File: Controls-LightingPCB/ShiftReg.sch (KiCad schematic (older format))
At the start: 1 part, among them U21 MCP23S17_SO

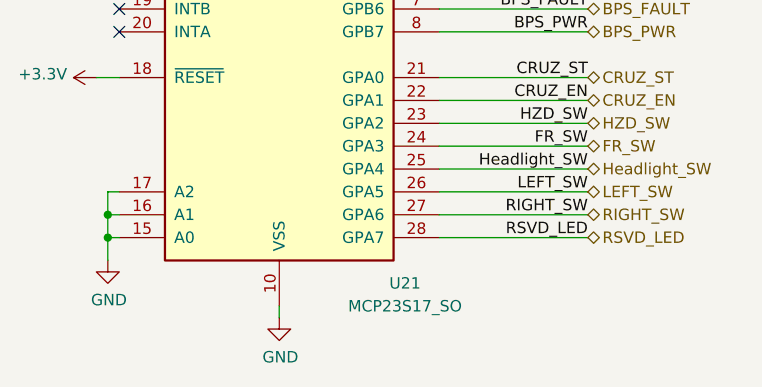
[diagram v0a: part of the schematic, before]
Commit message: Added hierarchical sheets and connections
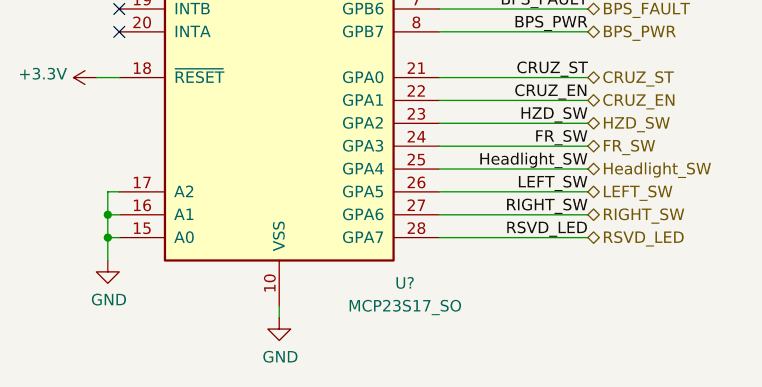
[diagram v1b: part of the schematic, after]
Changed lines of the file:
@@
 $Descr A4 11693 8268
 encoding utf-8
-Sheet 11 11
+Sheet 3 4
 Title ""
 Date ""
@@
 AR Path="/5F79C078" Ref="U?"  Part="1"
 AR Path="/5F768F42/5F79C078" Ref="U21"  Part="1"
-F 0 "U21" H 6400 3100 50  0000 C CNN
+AR Path="/5F78B6DA/5F79C078" Ref="U?"  Part="1"
+F 0 "U?" H 6400 3100 50  0000 C CNN
 F 1 "MCP23S17_SO" H 6400 3000 50  0000 C CNN
 F 2 "Package_SO:SOIC-28W_7.5x17.9mm_P1.27mm" H 6050 3100 50  0001 L CNN
@@
 	6550 3400 7200 3400
 $Comp
-L power:+3.3V #PWR015
+L power:+3.3V #PWR?
 U 1 1 5F7B1848
 P 5850 2950
-F 0 "#PWR015" H 5850 2800 50  0001 C CNN
+F 0 "#PWR?" H 5850 2800 50  0001 C CNN
 F 1 "+3.3V" H 5865 3123 50  0000 C CNN
 F 2 "" H 5850 2950 50  0001 C CNN
@@
 $EndComp
 $Comp
-L power:GND #PWR016
+L power:GND #PWR?
 U 1 1 5F7B1F8F
 P 5850 5250
-F 0 "#PWR016" H 5850 5000 50  0001 C CNN
+F 0 "#PWR?" H 5850 5000 50  0001 C CNN
 F 1 "GND" H 5855 5077 50  0000 C CNN
 F 2 "" H 5850 5250 50  0001 C CNN
@@
 Connection ~ 5100 4900
 $Comp
-L power:GND #PWR014
+L power:GND #PWR?
 U 1 1 5F7E0854
 P 5100 5000
-F 0 "#PWR014" H 5100 4750 50  0001 C CNN
+F 0 "#PWR?" H 5100 4750 50  0001 C CNN
 F 1 "GND" H 5105 4827 50  0000 C CNN
 F 2 "" H 5100 5000 50  0001 C CNN
@@
 $EndComp
 $Comp
-L power:+3.3V #PWR013
+L power:+3.3V #PWR?
 U 1 1 5F7E23AF
 P 5050 4200
-F 0 "#PWR013" H 5050 4050 50  0001 C CNN
+F 0 "#PWR?" H 5050 4050 50  0001 C CNN
 F 1 "+3.3V" V 5065 4328 50  0000 L CNN
 F 2 "" H 5050 4200 50  0001 C CNN
